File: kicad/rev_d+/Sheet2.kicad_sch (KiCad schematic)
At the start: 186 parts, among them J10 vg_old, J6 JUMPER, J8 JUMPER, J9 JUMPER, Q2 QUARTZ, Q3 QUARTZ32768, X11 KEYB-MOUSE, X12 IDC20, X13 USB_C, X15 PLB2-2, X19 AVR pgm conn, X21 Turbosound conn, X22 PS2 extra input, X23 SEGA pads, X25 external clock, X3 IDC26LPT, X4 IDC10M, X5 IDC10M, X6 RS232_9

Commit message: pentevo: rev D+: start replacing MCU
git-svn-id: svn://localhost/local-pentevo@1289 c6c76956-fad2-4150-a3a9-ea0a427205ba
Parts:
- removed C40: 0.1uF, C-CHIP, symbol eva-altium-import:Sheet2_0_CAPCHIP
- removed C60: 10uF X7R, Capacitor_SMD:C_1206_3216Metric_Pad1.33x1.80mm_HandSolder, symbol eva-altium-import:Sheet2_0_CAPCHIP
- removed C84, C85: 0.1uF, C-CHIP, symbol eva-altium-import:Sheet2_3_CAPCHIP
- removed D15: PCF8583P, DIP8, symbol eva-altium-import:Sheet2_0_PCF8583P
- removed D15*: PCF8583T, PCF8583T, symbol eva-altium-import:Sheet2_0_PCF8583T
- removed D4: ATMEGA128, TQFP64X8, symbol eva-altium-import:Sheet2_0_ATMEGA128
- removed R101: 1K, R-CHIP, symbol eva-altium-import:Sheet2_1_RESCHIP
- removed R22, R23: 4K7, R-CHIP, symbol eva-altium-import:Sheet2_1_RESCHIP
- removed R24: 10K, R-CHIP, symbol eva-altium-import:Sheet2_1_RESCHIP
- removed R25: 1K, R-CHIP, symbol eva-altium-import:Sheet2_0_RESCHIP
- removed R30: 10K, R-CHIP, symbol eva-altium-import:Sheet2_2_RESCHIP
- removed VD4, VD5: LL4148, Diode_SMD:D_MiniMELF_Handsoldering, symbol eva-altium-import:Sheet2_0_LL4148
- removed X25: external clock, Connector_PinHeader_2.54mm:PinHeader_1x01_P2.54mm_Vertical, symbol Connector:Conn_01x01_Pin
- added D4: ~, symbol eva-altium-import:CH32V317VCT6
- added R25: 1K, R-CHIP, symbol eva-altium-import:Sheet2_1_RESCHIP
- C39: value 0.1uF -> 12pF
- C7: value 6.8pF -> 12pF
- Q2: ALTIUM_VALUE 11.059Mhz -> 8.000Mhz
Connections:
- net RTC_X2 is gone; now on an unnamed net: Q3.2
- net GND: now also C39.1, C7.1, D4.10 (GND), D4.19 (GNDA), D4.20 (V_{REF}-), D4.27 (GND), D4.41 (GND), D4.47 (GND), D4.7 (PC13/TAMPER), D4.74 (GND), D4.99 (GND); no longer C39.2
- net at C4.2, Q2.A: now also D4.12 (oscin)
- net at C5.2, Q2.B: now also D4.13 (oscout)
- net at GB1.1 (PLUS): now also C6.2, C9.1, D4.6 (V_{BAT})
- removed net RTC_PWR: C6.2, C7.1, C9.1
- net RTC_X1: no longer names the net of C7.2
- net RTC_X1: now also D4.8 (PC14/osc32in); no longer Q3.1
- net VCC5_MEGA renamed VCC5_MCU
- net VCC5_MCU: no longer C39.1
- new net: C39.2, D4.9 (PC15/osc32out), Q3.1
- new net VCC33_MCU: D4.100 (V_{IO}), D4.11 (V_{CC}), D4.21 (V_{REF}+), D4.22 (V_{CC}A), D4.28 (V_{IO}), D4.48 (V_{IO}), D4.51 (V_{CC}), D4.75 (V_{CC})
- no-connect marks 38 -> 37
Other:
- note removed: "RTC in SOP package"
- moved on the sheet: C105, C36, C37, C4, C5, C50, C6, C82, C83, C9, D20A, D20B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

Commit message: pentevo: rev D+:
git-svn-id: svn://localhost/local-pentevo@1291 c6c76956-fad2-4150-a3a9-ea0a427205ba
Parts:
- added J12, J5: JUMPER, JUMPER, symbol eva-altium-import:Sheet2_3_JUMPER
- added R22, R23: 10K, R-CHIP, symbol eva-altium-import:Sheet2_0_mirrored_RESCHIP
- added R24, R30: 5K1, R-CHIP, symbol eva-altium-import:Sheet2_0_RESCHIP
- R153, R160: value 1K -> 10K
- R26: value 1K -> 5K1
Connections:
- net GND: now also R22.2 (i/o1), R23.2 (i/o1)
- net VCC33_MCU: now also R153.1 (i/o), R26.2 (i/o1), J12.1 (2), J5.1 (2)
- net VCC5_MCU: no longer R153.2 (i/o1), R26.2 (i/o1)
- net ~{PRGRST}: no longer C8.2, R26.1 (i/o), VT2.3 (collector)
- net at J9.1 (2): now also R153.2 (i/o1); no longer R153.1 (i/o)
- net at D4.14 (NRST): now also C8.2, R26.1 (i/o), VT2.3 (collector)
- net at D4.37 (BOOT1): now also R24.1 (i/o)
- net at D4.94 (BOOT0): now also R30.1 (i/o)
- new net: J5.0 (1), R22.1 (i/o), R30.2 (i/o1)
- new net: J12.0 (1), R23.1 (i/o), R24.2 (i/o1)
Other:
- moved on the sheet: C38, C8, J9, R153, R160, R25, R26, R31, R35, VD6, VT2

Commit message: pentevo: rev D+: add pgm connector, add eth rj45 connector
git-svn-id: svn://localhost/local-pentevo@1293 c6c76956-fad2-4150-a3a9-ea0a427205ba
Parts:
- added C40, C60: 1uF, C-CHIP, symbol eva-altium-import:Sheet2_1_CAPCHIP
- added J13: RJ45_Hanrun_HR911105A_Horizontal, Connector_RJ:RJ45_Hanrun_HR911105A_Horizontal, symbol Connector:RJ45_Hanrun_HR911105A_Horizontal
- X19: value AVR pgm conn -> WCH LinkE pgm conn
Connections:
- net GND: now also C40.2, C60.2, J13.8; no longer X19.10 (Pin_10), X19.4 (Pin_4)
- net PRGDI_RXD: no longer X19.1 (Pin_1)
- net PRGDO_TXD: no longer X19.9 (Pin_9)
- net SHIELD: now also J13.SH
- net SPICK: no longer X19.7 (Pin_7)
- net VCC5_MCU: no longer X19.2 (Pin_2)
- net ~{PGM_DETECT}: no longer X19.8 (Pin_8)
- net MDITP: now reaches D4.42 (MDITP)
- net MDITP: now also J13.1 (TD+)
- net MDITN: now reaches D4.43 (MDITN)
- net MDITN: now also J13.2 (TD-)
- net MDIRP: now reaches D4.44 (MDIRP)
- net MDIRP: now also J13.3 (RD+)
- net MDIRN: now reaches D4.45 (MDIRN)
- net MDIRN: now also J13.6 (RD-)
- net PGM_RX: now reaches D4.68 (PA9)
- net PGM_RX: now also X19.3 (Pin_3)
- net PGM_TX: now reaches D4.69 (PA10)
- net PGM_TX: now also X19.1 (Pin_1)
- net PGM_SWCLK: now reaches D4.72 (SWDIO)
- net PGM_SWCLK: now also X19.2 (Pin_2)
- net PGM_SWDIO: now reaches D4.76 (SWCLK)
- net PGM_SWDIO: now also X19.4 (Pin_4)
- net ~{PRGRST}: no longer names the net of X19.5 (Pin_5)
- new net: C40.1, J13.4 (TCT)
- new net: C60.1, J13.5 (RCT)
- no-connect marks 37 -> 36
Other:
- moved on the sheet: X19

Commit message: pentevo: rev D+: 3v3 to pgm connector, power pins/caps, eth leds
git-svn-id: svn://localhost/local-pentevo@1294 c6c76956-fad2-4150-a3a9-ea0a427205ba
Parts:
- added C132, C133, C141, C142, C143, C144, C85: 0.1uF, C-CHIP, symbol eva-altium-import:Sheet2_2_CAPCHIP
- added C146: 10uF, EC-CHIP, symbol eva-altium-import:Sheet2_3_ECAPCHIP
- added C147: 0.1uF, C-CHIP, symbol eva-altium-import:Sheet2_1_CAPCHIP
- added C84: 1uF, C-CHIP, symbol eva-altium-import:Sheet2_1_CAPCHIP
- added L5: 220 nH bead, L-CHIP, symbol eva-altium-import:Sheet1_1_L-CHIP
- added R101, R142: 390, R-CHIP, symbol eva-altium-import:Sheet2_0_RESCHIP
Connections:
- net GND: now also J13.10, C132.2, C133.2, C141.2, C142.2, C143.2, C144.2, C146.2, C147.1, C84.1, C85.2
- net PGM_RX: now also D4.69 (PA10); no longer D4.68 (PA9)
- net PGM_TX: now also D4.68 (PA9); no longer D4.69 (PA10)
- net VCC33_MCU: now also D4.46 (V_{CC}ETH), J13.12, X19.8 (Pin_8), C132.1, C133.1, C141.1, C142.1, C143.1, C144.1, C85.1, L5.2; no longer D4.21 (V_{REF}+), D4.22 (V_{CC}A)
- net at J13.11: now also R101.2 (i/o1)
- net at J13.9: now also R142.2 (i/o1)
- net ETH_LED0: now reaches D4.38 (LED0)
- net ETH_LED0: now also R101.1 (i/o)
- net ETH_LED1: now reaches D4.39 (LED1)
- net ETH_LED1: now also R142.1 (i/o)
- net at D4.40 (V_{DD}K): now also C84.2
- new net: C146.1, C147.2, D4.21 (V_{REF}+), D4.22 (V_{CC}A), L5.1
- no-connect marks 36 -> 40
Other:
- moved on the sheet: C40, C6, C60, C9, GB1, J13

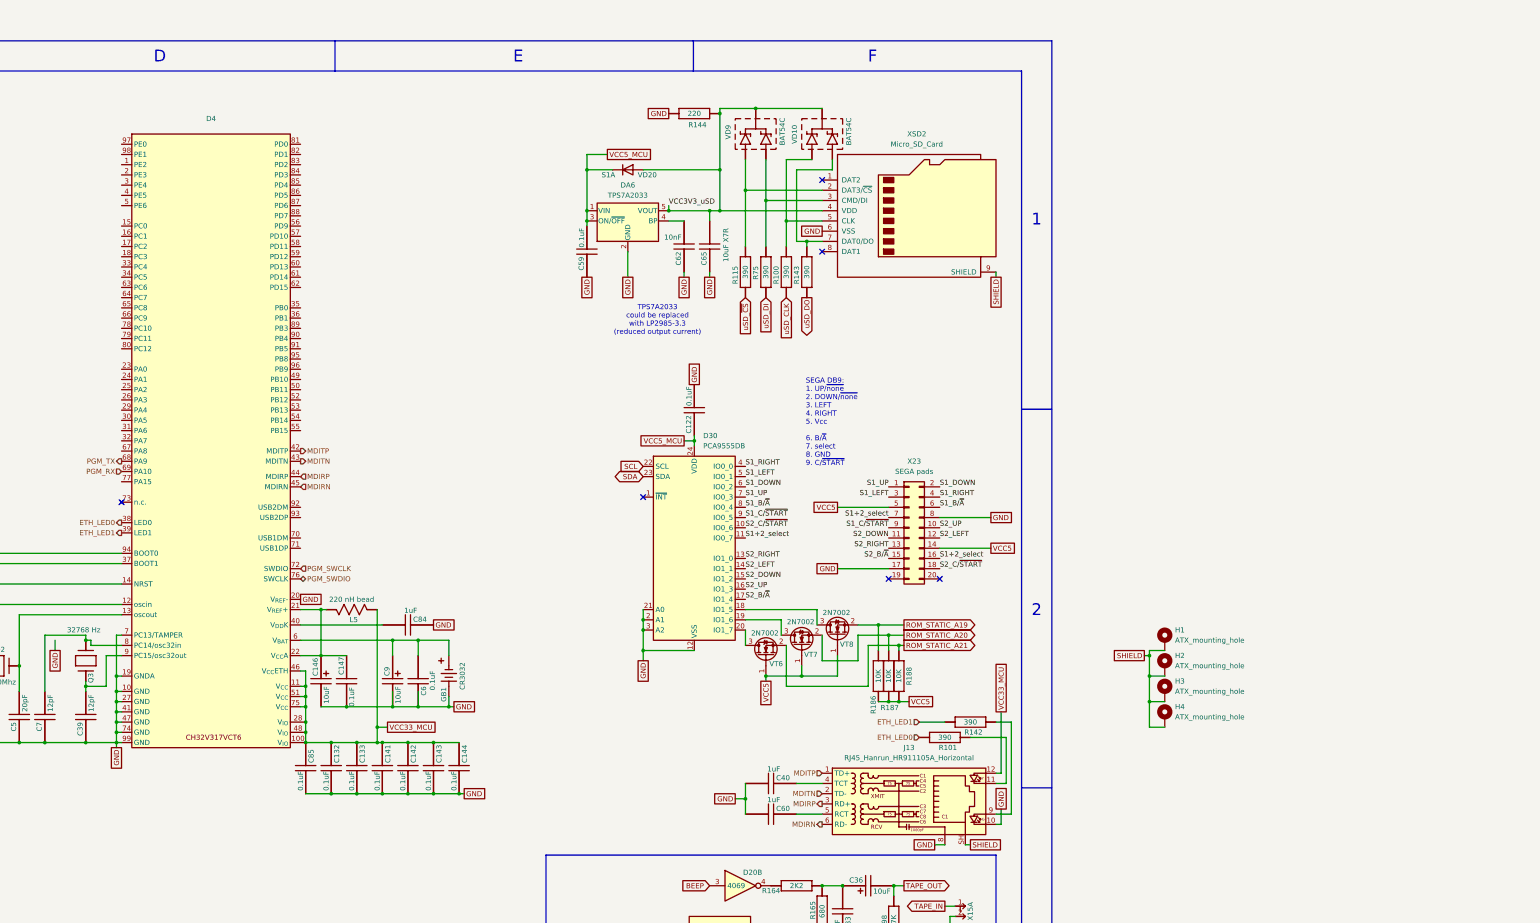
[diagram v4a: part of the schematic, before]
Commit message: pentevo: rev D+: connect uSD
git-svn-id: svn://localhost/local-pentevo@1297 c6c76956-fad2-4150-a3a9-ea0a427205ba
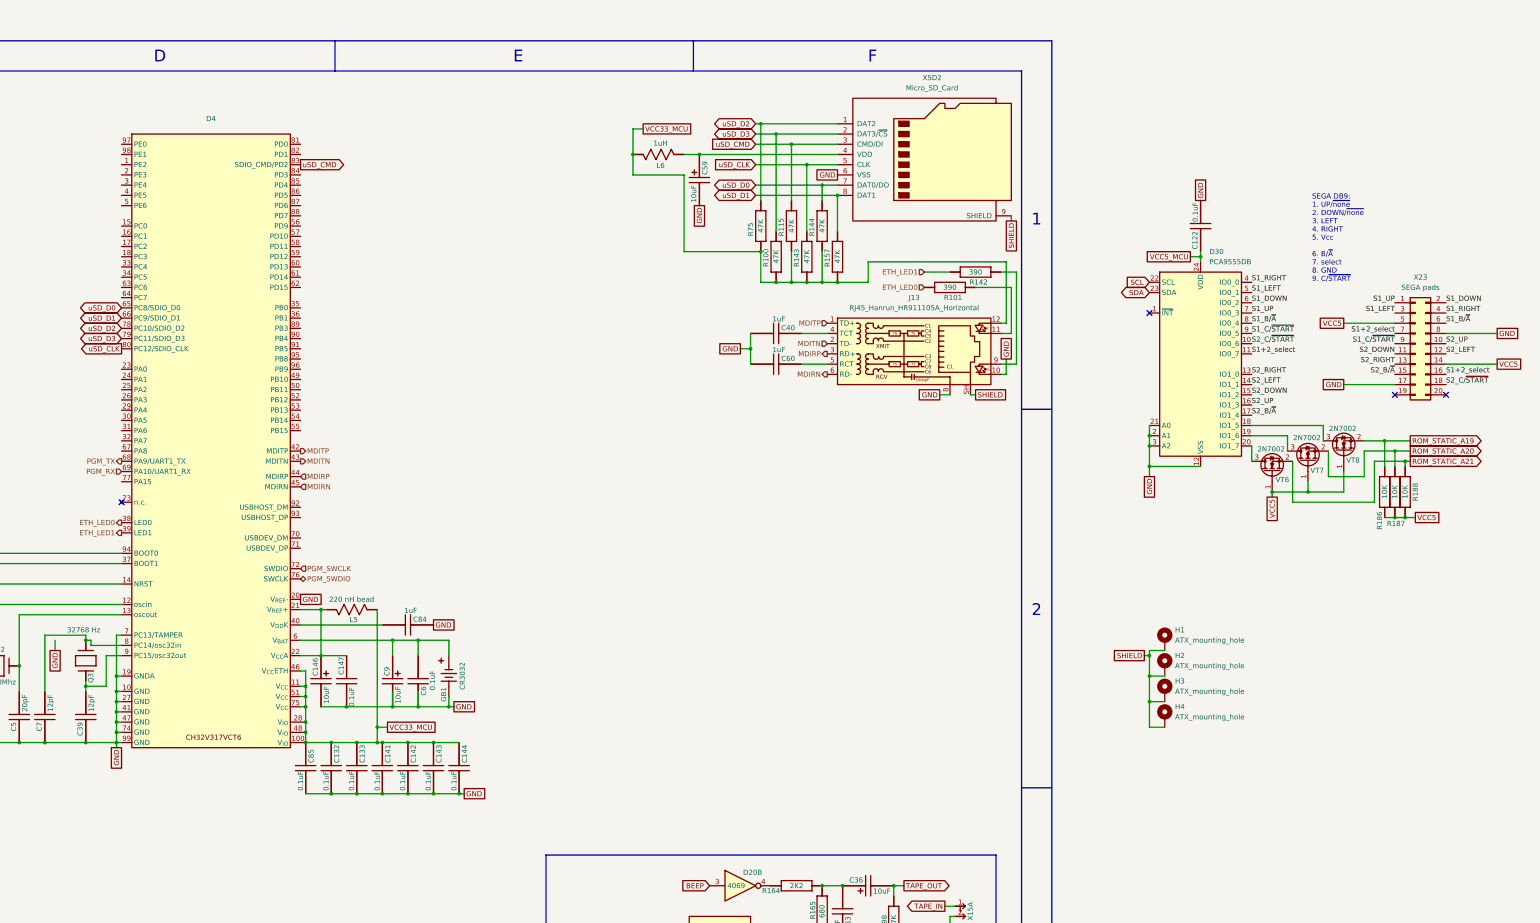
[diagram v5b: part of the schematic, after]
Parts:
- removed C59: 0.1uF, C-CHIP, symbol eva-altium-import:Sheet2_0_CAPCHIP
- removed C62: 10nF, C-CHIP, symbol eva-altium-import:Sheet2_1_CAPCHIP
- removed C65: 10uF X7R, Capacitor_SMD:C_1206_3216Metric_Pad1.33x1.80mm_HandSolder, symbol eva-altium-import:Sheet2_0_CAPCHIP
- removed DA6: TPS7A2033, Package_TO_SOT_SMD:SOT-23-5_HandSoldering, symbol Regulator_Linear:LP2985-3.3
- removed R144: 220, R-CHIP, symbol eva-altium-import:Sheet1_0_RESCHIP
- removed VD10, VD9: BAT54C, SOT-23, symbol eva-altium-import:Sheet2_3_BAT54C
- removed VD20: S1A, Diode_SMD:D_SMA, symbol Diode:US1A
- added C59: 10uF, EC-CHIP, symbol eva-altium-import:Sheet1_0_ECAPCHIP
- added L6: 1uH, L-CHIP, symbol eva-altium-import:Sheet1_1_L-CHIP
- added R144, R157: 47K, R-CHIP, symbol eva-altium-import:Sheet2_0_RESCHIP
- R100, R115, R143, R75: value 390 -> 47K
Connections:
- net GND: now also C59.2
- net VCC33_MCU: now also R100.1 (i/o), R115.1 (i/o), R143.1 (i/o), R75.1 (i/o), L6.1, R144.1 (i/o), R157.1 (i/o)
- net uSD_CLK: now also D4.80 (PC12/SDIO_CLK), R143.2 (i/o1), XSD2.5 (CLK); no longer R100.2 (i/o1)
- net uSD_DI: no longer R75.2 (i/o1)
- net uSD_DO: no longer R143.2 (i/o1)
- net uSD_~{CS}: no longer R115.2 (i/o1)
- net uSD_D3: now reaches XSD2.2 (DAT3/~{CS})
- net uSD_D3: now also D4.79 (PC11/SDIO_D3), R100.2 (i/o1); no longer R115.1 (i/o)
- net uSD_CMD: now reaches XSD2.3 (CMD/DI)
- net uSD_CMD: now also D4.83 (SDIO_CMD/PD2), R115.2 (i/o1); no longer R75.1 (i/o)
- net uSD_D0: now reaches XSD2.7 (DAT0/DO)
- net uSD_D0: now also D4.65 (PC8/SDIO_D0), R144.2 (i/o1); no longer R143.1 (i/o)
- net uSD_D1: now reaches D4.66 (PC9/SDIO_D1)
- net uSD_D1: now also XSD2.8 (DAT1), R157.2 (i/o1)
- net uSD_D2: now reaches D4.78 (PC10/SDIO_D2)
- net uSD_D2: now also R75.2 (i/o1), XSD2.1 (DAT2)
- net VCC3V3_uSD: no longer names the net of XSD2.4 (VDD)
- net VCC3V3_uSD: now also C59.1, L6.2
- no-connect marks 40 -> 38
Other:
- note removed: "TPS7A2033 could be replaced with LP2985-3.3 (reduced output current)"
- moved on the sheet: C122, C40, C60, D30, J13, R101, R142, R186, R187, R188, VT6, VT7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

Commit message: pentevo: rev D+: usbhost, usbdevice, usbuart
git-svn-id: svn://localhost/local-pentevo@1300 c6c76956-fad2-4150-a3a9-ea0a427205ba
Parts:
- removed C55: 0.1uF, C-CHIP, symbol eva-altium-import:Sheet2_3_CAPCHIP
- removed unit 1 of D22
- removed unit 1 of D23
- removed R73: 10K, R-CHIP, symbol eva-altium-import:Sheet2_2_RESCHIP
- added D13: 74HCT125, symbol 74xx:74LS125
- added D15: 74HC14, symbol 74xx:74HC14
- added R158, R159, R199, R200: 5K1, R-CHIP, symbol eva-altium-import:Sheet2_0_mirrored_RESCHIP
- added X25: USB_C device, symbol Connector:USB_C_Receptacle_USB2.0_14P
- added X27: USB_A, symbol Connector:USB_A
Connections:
- net GND: now also R158.2 (i/o1), R159.2 (i/o1), X25.A1 (GND), X25.A12 (GND), X25.B1 (GND), X25.B12 (GND), X27.4 (GND)
- net PGM_RX: now also D4.67 (PA8/USART1_RX); no longer D4.69 (PA10/UART1_RX)
- net PGM_TX: now also D4.55 (USART1_TX/PB15); no longer D4.68 (PA9/UART1_TX)
- net SHIELD: now also X25.S1 (SHIELD), X27.5 (Shield)
- net VCC33_MCU: now also C57.1, D9.5 (VCC), D9.8 (V3), R199.1 (i/o), R200.1 (i/o)
- net VCC5_MCU: now also X27.1 (VBUS); no longer C57.1, D9.5 (VCC)
- net ZX_UART_TX: now reaches D4.49 (USART3_TX/PB10)
- net ZX_UART_RX: now reaches D4.50 (USART3_RX/PB11)
- net ZX_UART_CTS: now reaches D4.53 (USART3_CTS/PB13)
- net ZX_UART_RTS: now reaches D4.54 (USART3_RTS/PB14)
- net USBDEV-: now reaches D4.70 (USBDEV_DM)
- net USBDEV-: now also X25.A7 (D-), X25.B7 (D-)
- net USBDEV+: now reaches D4.71 (USBDEV_DP)
- net USBDEV+: now also X25.A6 (D+), X25.B6 (D+)
- net USBHOST-: now reaches D4.92 (USBHOST_DM)
- net USBHOST-: now also X27.2 (D-)
- net USBHOST+: now reaches D4.93 (USBHOST_DP)
- net USBHOST+: now also X27.3 (D+)
- new net: R159.1 (i/o), X25.A5 (CC1)
- new net: D4.68 (PA9/OTG_VBUS), R200.2 (i/o1)
- new net: R158.1 (i/o), X25.B5 (CC2)
- new net: X25.A4 (VBUS), X25.A9 (VBUS), X25.B4 (VBUS), X25.B9 (VBUS)
- new net: D4.69 (PA10/OTG_ID), R199.2 (i/o1)
- no-connect marks 38 -> 39
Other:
- note added: "device USB"
- note added: "host USB"
- moved on the sheet: C105, C36, C37, C57, C83, D20A, D20B, D20C, D20D, D20E, D20F, D20G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

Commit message: pentevo: rev D+: zx uart, dbg uart
git-svn-id: svn://localhost/local-pentevo@1301 c6c76956-fad2-4150-a3a9-ea0a427205ba
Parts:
- removed D15, D23: 74HC14, symbol 74xx:74HC14
- removed R176: 390, R-CHIP, symbol eva-altium-import:Sheet2_0_mirrored_RESCHIP
- added R73: 5K1, R-CHIP, symbol eva-altium-import:Sheet2_2_RESCHIP
- D13: value 74HCT125 -> 74HC125
- D13: renamed from D22; value 74HCT125 -> 74HC125
- D16: value MAX232 -> MAX3232
- R74: value 10K -> 5K1
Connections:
- net CTS_AVR: no longer D13.8, R71.2 (i/o1)
- net GND: now also R73.2 (i/o1)
- net PRGDO_TXD: no longer D13.12, R4.1 (i/o)
- net RTS_AVR: no longer D16.10 (T2in), R21.2 (i/o1)
- net RXD_DBG: no longer D9.6 (TXD)
- net TXD_DBG: no longer D9.7 (RXD)
- net VCC33_MCU: now also C20.2, C56.1, D13.12, D13.13, D13.14 (VCC), D13.2, D16.16 (VCC), R74.2 (i/o1), X5.4
- net VCC5: no longer C20.2, D16.16 (VCC), X5.4
- net VCC5_MCU: no longer C56.1, D13.14 (VCC), R74.2 (i/o1)
- net ZX_UART_CTS: now also D13.8, R71.2 (i/o1)
- net ZX_UART_RTS: now also D16.10 (T2in), R21.2 (i/o1)
- net ZX_UART_RX: now also D13.6, R72.2 (i/o1)
- net ZX_UART_TX: now also D16.11 (T1in), R4.1 (i/o)
- net ~{TTL_DETECT}: now also D13.1
- net at D13.10, D13.4: now also D13.3, R73.1 (i/o)
- net DBG_TX: now reaches D4.15 (PC0/UART6_TX)
- net DBG_TX: now also D9.7 (RXD)
- net DBG_RX: now reaches D4.16 (PC1/UART6_RX)
- net DBG_RX: now also D9.6 (TXD)
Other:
- moved on the sheet: C111, C112, C113, C114, C115, C16, C17, C18, C19, C20, C56, D13B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

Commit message: pentevo: rev D+: PS/2 WIP
git-svn-id: svn://localhost/local-pentevo@1302 c6c76956-fad2-4150-a3a9-ea0a427205ba
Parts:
- removed C82: 0.1uF, C-CHIP, symbol eva-altium-import:Sheet2_0_CAPCHIP
- removed R31: 10K, R-CHIP, symbol eva-altium-import:Sheet2_0_mirrored_RESCHIP
- added C55, C62: 0.1uF, C-CHIP, symbol eva-altium-import:Sheet2_3_mirrored_CAPCHIP
- added D15, D22: 74HCT125, symbol 74xx:74LS125
- added R176, R201, R202, R31: 5K1, R-CHIP, symbol eva-altium-import:Sheet2_0_RESCHIP
- R73, R74: value 5K1 -> 10K
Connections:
- net GND: now also C55.2, C62.2, D15.12, D15.2, D15.5, D15.7 (GND), D15.9, D22.12, D22.2, D22.5, D22.7 (GND), D22.9
- net PS2_KEYB_CLK: now also R123.2 (i/o1), D15.1, D15.6; no longer R124.1 (i/o)
- net PS2_KEYB_DAT: now also R124.2 (i/o1), D15.10, D15.11; no longer R123.1 (i/o)
- net PS2_MOUS_CLK: now also R125.2 (i/o1), D22.1, D22.6; no longer R126.1 (i/o)
- net PS2_MOUS_DAT: now also R126.2 (i/o1), D22.10, D22.11; no longer R125.1 (i/o)
- net SCL: now also D4.95 (SCL/PB8)
- net SDA: now also D4.96 (SDA/PB9)
- net SPICK: now also D4.30 (PA5/SPICK)
- net SPIDI: now also D4.31 (PA6/MISO)
- net SPIDO: now also D4.32 (PA7/MOSI)
- net VCC33_MCU: now also VD6.A, R176.2 (i/o1), R201.2 (i/o1), R202.2 (i/o1), R31.1 (i/o)
- net VCC5: now also R123.1 (i/o), R124.1 (i/o), R125.1 (i/o), R126.1 (i/o); no longer R123.2 (i/o1), R124.2 (i/o1), R125.2 (i/o1), R126.2 (i/o1)
- net VCC5_MCU: now also C55.1, C62.1, D15.14 (VCC), D22.14 (VCC); no longer VD6.A
- net ~{SPICS}: now also D4.29 (PA4/SPI~{CS})
- new net PS2_KB_CLK_I: D15.3, R176.1 (i/o)
- new net PS2_KB_CLK_O: D15.4
- new net PS2_KB_DAT_I: D15.8, R31.2 (i/o1)
- new net PS2_KB_DAT_O: D15.13
- new net PS2_MS_CLK_I: D22.3, R201.1 (i/o)
- new net PS2_MS_CLK_O: D22.4
- new net PS2_MS_DAT_I: D22.8, R202.1 (i/o)
- new net PS2_MS_DAT_O: D22.13
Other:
- note added: "PS/2 kbd+mouse"
- note removed: "Real Time Counter"
- moved on the sheet: C10, C11, C111, C112, C113, C114, C115, C13, C14, C15, C16, C17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
